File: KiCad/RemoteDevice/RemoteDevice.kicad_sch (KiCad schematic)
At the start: 43 parts, among them J1 Alim, J2 CN1, Q1 Si4435, SW1 BP, SW2 BP, U1 XC9140, U2 STM32L041F6Px, U3 MCP6281, U4 ADT7410TRZ, U5 MCP6281, U6 RT606, U7 Microphone

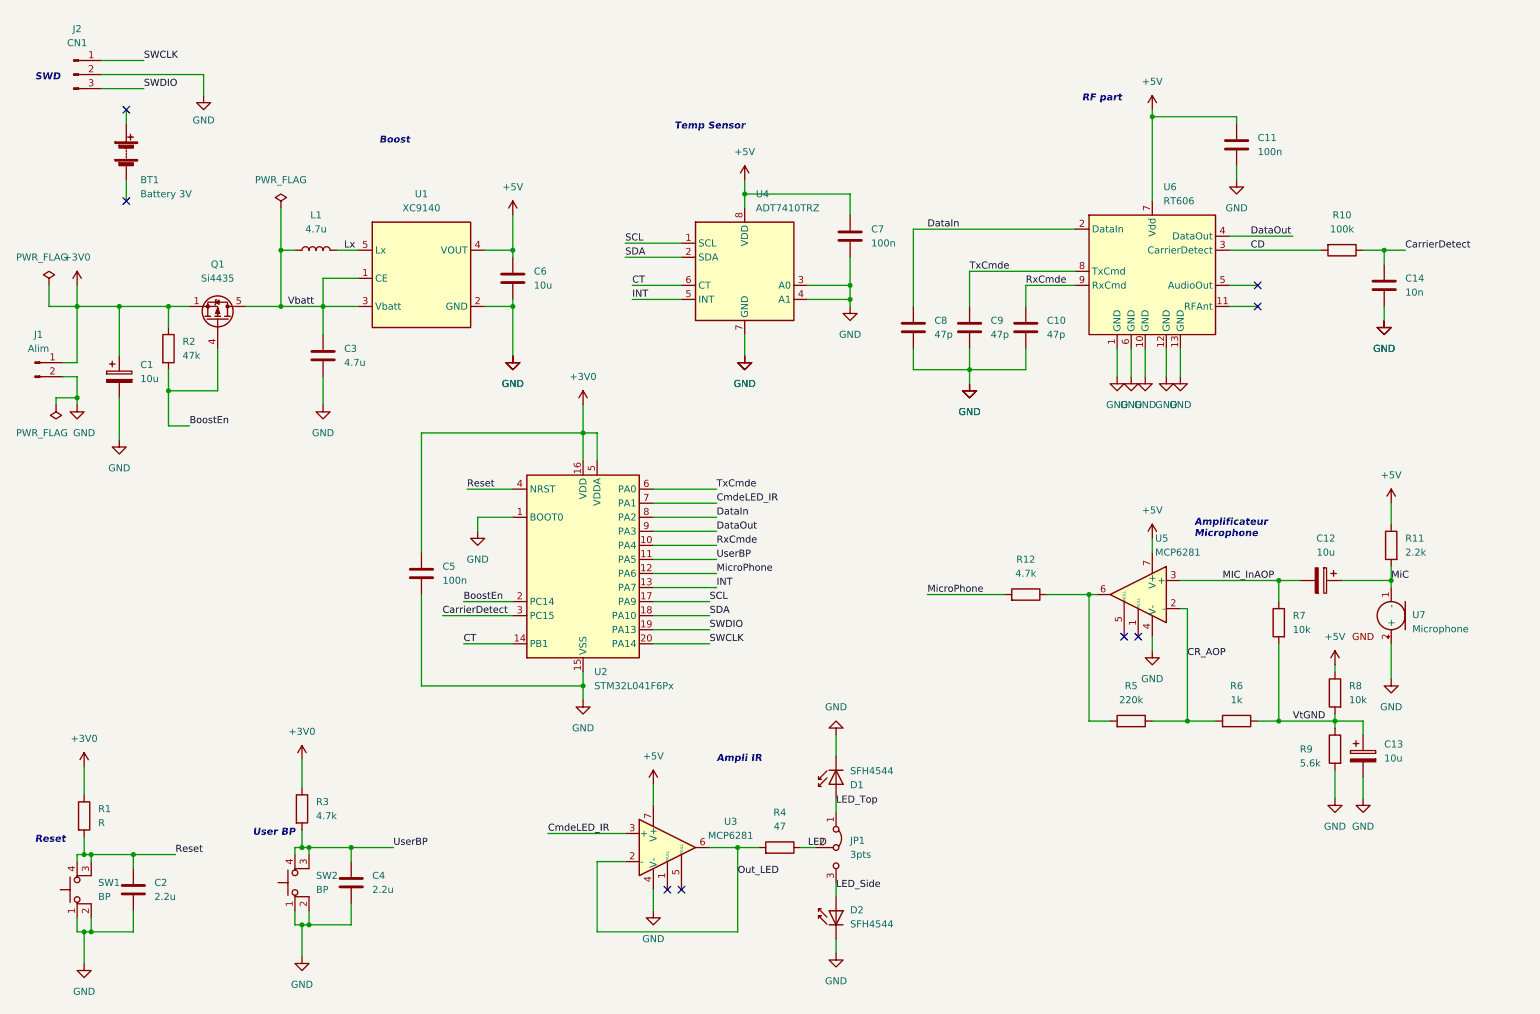
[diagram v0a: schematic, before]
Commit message: modifs schéma faites, reste à faire l'association pour la netlist. Il manque aussi le Xbee
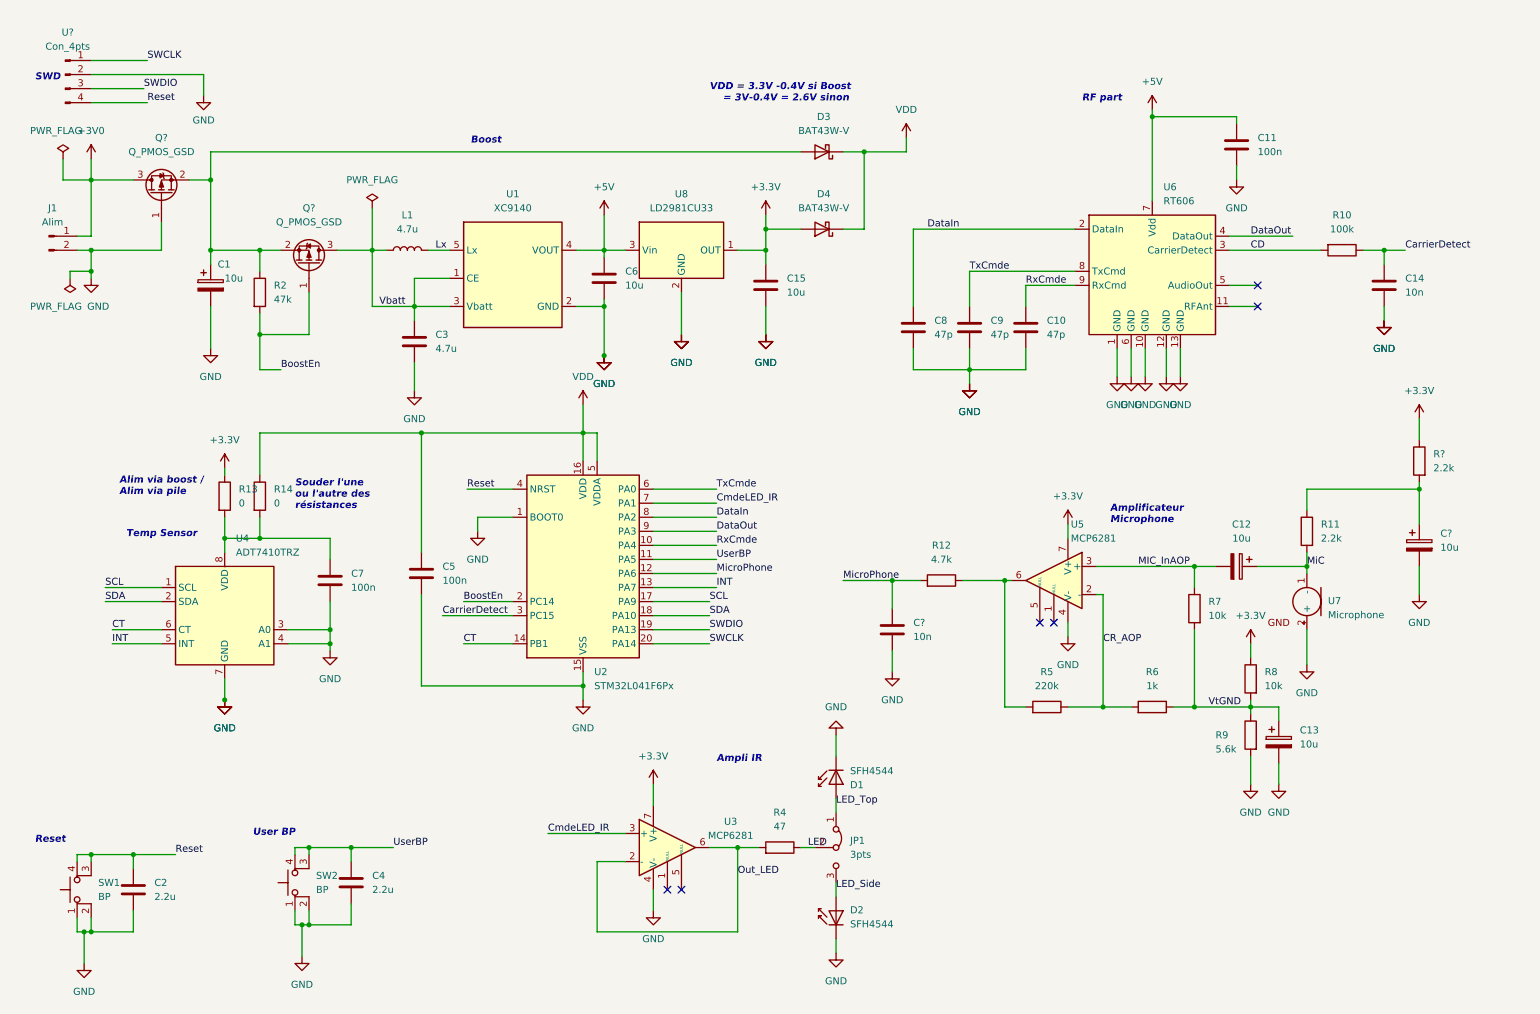
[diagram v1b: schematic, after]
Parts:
- removed BT1: Battery 3V, Battery:BatteryHolder_Keystone_2468_2xAAA, symbol Device:Battery
- removed J2: CN1, LibKiCad_PjtDeviceManagePV:PinHeader3pts, symbol Connector:Conn_01x03_Male
- removed Q1: Si4435, Package_SO:PowerPAK_SO-8_Single, symbol Transistor_FET:Si7141DP
- removed R1: R, Resistor_SMD:R_1206_3216Metric, symbol Device:R
- removed R3: 4.7k, Resistor_SMD:R_1206_3216Metric, symbol Device:R
- added C15: 10u, Capacitor_SMD:C_1812_4532Metric, symbol Device:C
- added C?: 10u, Capacitor_Tantalum_SMD:CP_EIA-7132-20_AVX-U, symbol Device:C_Polarized
- added C?: 10n, Capacitor_SMD:C_1206_3216Metric, symbol Device:C
- added D3, D4: BAT43W-V, Diode_SMD:D_SOD-123, symbol Diode:BAT43W-V
- added Q? (x2): Q_PMOS_GSD, symbol Device:Q_PMOS_GSD
- added R13, R14: 0, Resistor_SMD:R_1206_3216Metric, symbol Device:R
- added R?: 2.2k, Resistor_SMD:R_1206_3216Metric, symbol Device:R
- added U8: LD2981CU33, Package_TO_SOT_SMD:SOT-89-3_Handsoldering, symbol LibKiCad_PjtDeviceManagePV:LD2981CU33
- added U?: Con_4pts, LibKiCad_PjtDeviceManagePV:PinHeader4pts, symbol LibKiCad_PjtDeviceManagePV:Con_4pts
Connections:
- net +3V0: now also Q?.3 (D); no longer C1.1, C5.1, R2.1, U2.16 (VDD), U2.5 (VDDA)
- net +5V: now also U8.3 (Vin); no longer C7.1, R11.1, R8.1, U3.7 (V+), U4.8 (VDD), U5.7 (V+)
- net BoostEn: now also Q?.1 (G)
- net GND: now also C15.2, C?.2, C?.2, Q?.1 (G), U8.2 (GND), U?.2
- net MicroPhone: now also C?.1
- net Reset: now also U?.4
- net SWCLK: now also U?.1
- net SWDIO: now also U?.3
- net Vbatt: now also Q?.3 (D)
- new net: C7.1, R13.2, R14.2, U4.8 (VDD)
- new net: C?.1, R11.1, R?.2
- new net: C1.1, D3.2 (A), Q?.2 (S), Q?.2 (S), R2.1
- new net +3V3: C15.1, D4.2 (A), R13.1, R8.1, R?.1, U3.7 (V+), U5.7 (V+), U8.1 (OUT)
- new net VDD: C5.1, D3.1 (K), D4.1 (K), R14.1, U2.16 (VDD), U2.5 (VDDA)
- no-connect marks 8 -> 6
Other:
- note added: "Alim via boost / Alim via pile"
- note added: "Souder l'une ou l'autre des résistances"
- note added: "VDD = 3.3V -0.4V si Boost = 3V-0.4V = 2.6V sinon"
- moved on the sheet: C1, C12, C13, C3, C6, C7, J1, L1, R11, R12, R2, R5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

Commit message: schéma finalisé, prise en compte des modifs indiquées dans AfairePCB.txt. Prêt pour nouveau PCB
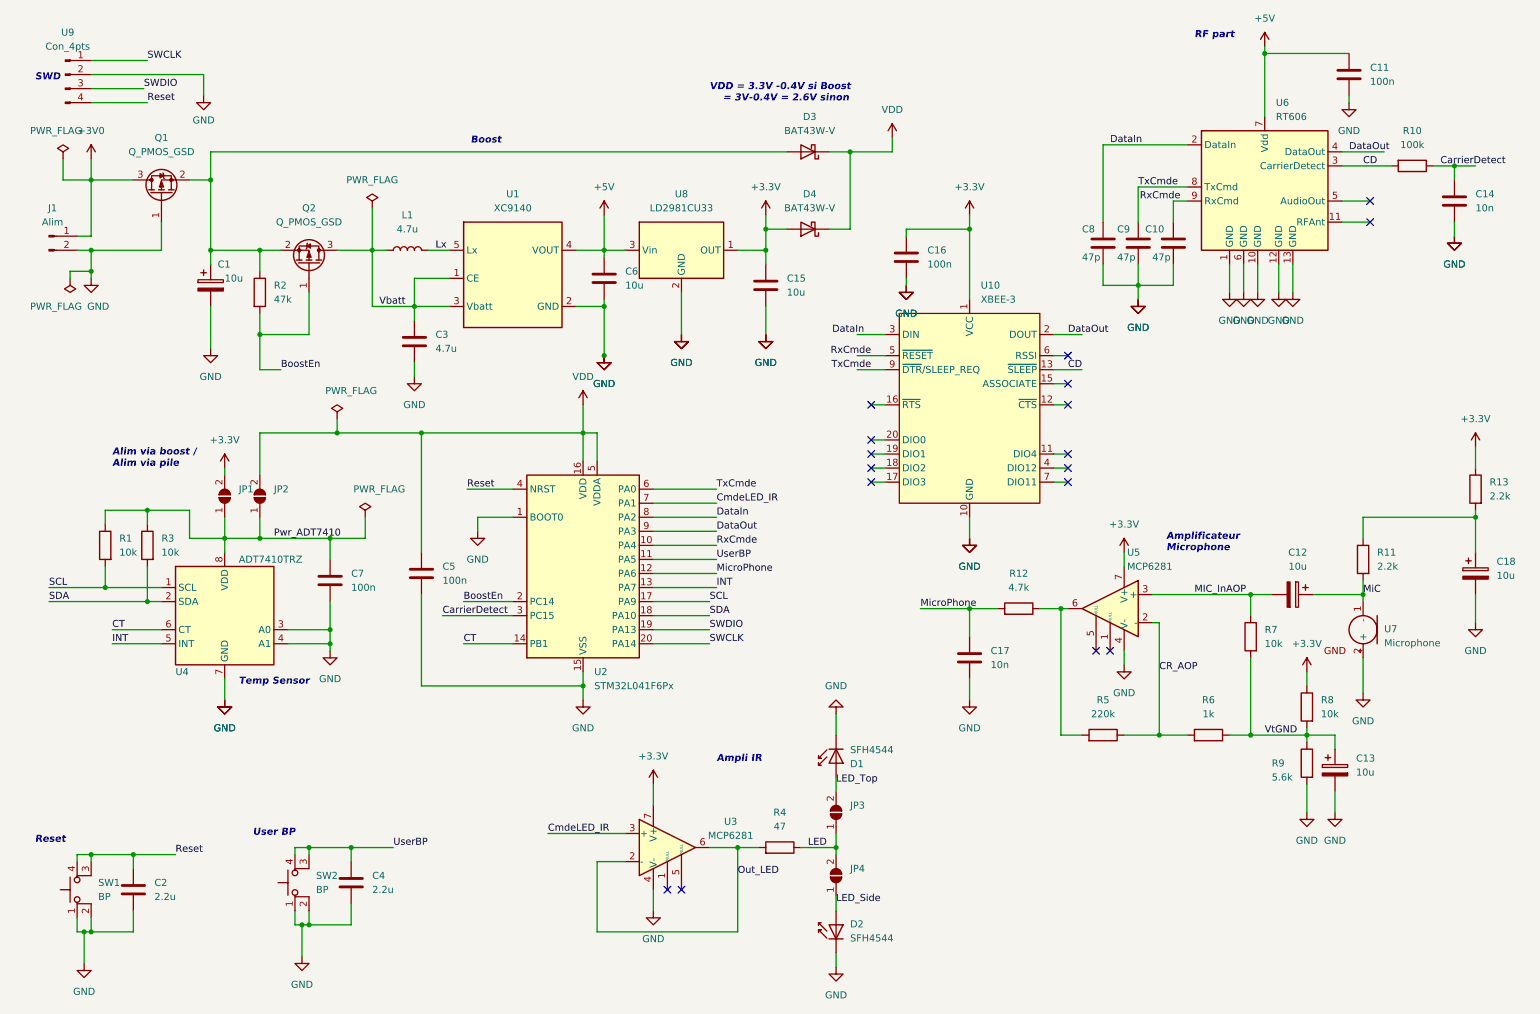
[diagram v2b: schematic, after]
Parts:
- removed JP1: 3pts, LibKiCad_PjtDeviceManagePV:PinHeader3pts, symbol Jumper:Jumper_3_Bridged12
- removed R13, R14: 0, Resistor_SMD:R_1206_3216Metric, symbol Device:R
- added C16: 100n, Capacitor_SMD:C_1206_3216Metric, symbol Device:C
- added JP1, JP2, JP3, JP4: SolderJumper_2_Open, Jumper:SolderJumper-2_P1.3mm_Open_TrianglePad1.0x1.5mm, symbol Jumper:SolderJumper_2_Open
- added R1, R3: 10k, Resistor_SMD:R_1206_3216Metric, symbol Device:R
- added U10: XBEE-3, INSA:XBEE-3-TH, symbol Insa:XBEE-3
- gave numbers to parts that had none: 6
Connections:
- net +3V3: now also C16.1, JP1.2 (B), U10.1 (VCC)
- net CD: now also U10.13 (~{SLEEP})
- net DataIn: now also U10.3 (DIN)
- net DataOut: now also U10.2 (DOUT)
- net GND: now also C16.2, U10.10 (GND)
- net LED: now also JP3.1 (A), JP4.2 (B)
- net LED_Side: now also JP4.1 (A)
- net LED_Top: now also JP3.2 (B)
- net RxCmde: now also U10.5 (~{RESET})
- net SCL: now also R1.2
- net SDA: now also R3.2
- net TxCmde: now also U10.9 (~{DTR}/SLEEP_REQ)
- net VDD: now also JP2.2 (B)
- net Pwr_ADT7410: now reaches C7.1, U4.8 (VDD)
- net Pwr_ADT7410: now also JP1.1 (A), JP2.1 (A), R1.1, R3.1
- no-connect marks 6 -> 17
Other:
- note removed: "Souder l'une ou l'autre des résistances"
- moved on the sheet: C10, C11, C12, C13, C14, C17, C18, C8, C9, D1, D2, D3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

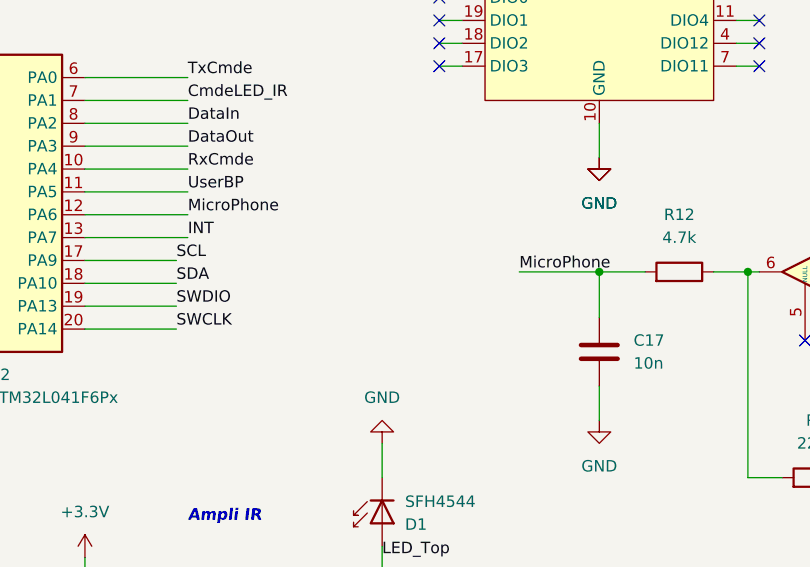
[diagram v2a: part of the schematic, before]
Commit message: routage commencé. ALim OK placer les deux diodes, étudier l'alim particulière uC et Temp Sensor
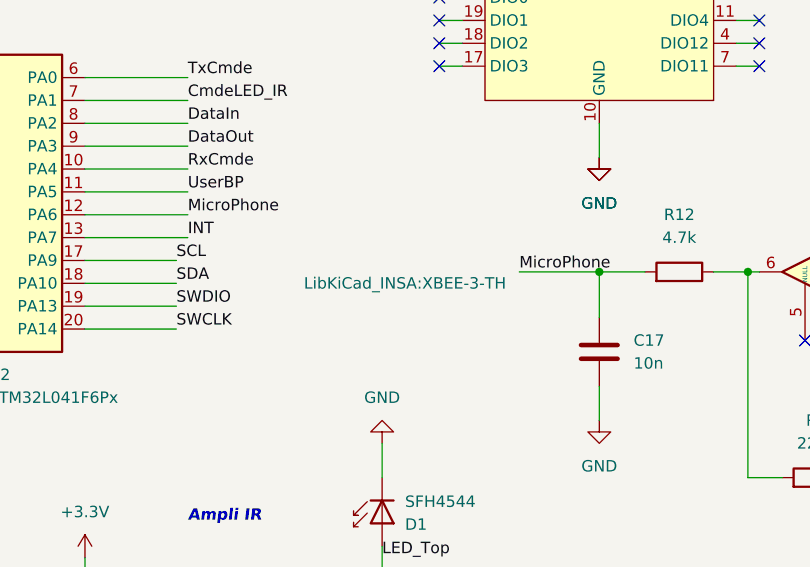
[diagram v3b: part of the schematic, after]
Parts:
- Q1, Q2: footprint (none) -> Package_TO_SOT_SMD:SOT-23
- U10: footprint INSA:XBEE-3-TH -> LibKiCad_INSA:XBEE-3-TH
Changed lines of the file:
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@@
       (effects (font (size 1.27 1.27)) (justify left))
     )
-    (property "Footprint" "INSA:XBEE-3-TH" (id 2) (at 163.83 123.19 0)
-      (effects (font (size 1.27 1.27)) hide)
-    )
+    (property "Footprint" "LibKiCad_INSA:XBEE-3-TH" (id 2) (at 163.83 123.19 0))
     (property "Datasheet" "" (id 3) (at 163.83 123.19 0)
       (effects (font (size 1.27 1.27)) hide)
@@
     (property "Reference" "Q1" (id 0) (at 39.37 36.83 90))
     (property "Value" "Q_PMOS_GSD" (id 1) (at 39.37 39.37 90))
-    (property "Footprint" "" (id 2) (at 36.83 41.91 0)
+    (property "Footprint" "Package_TO_SOT_SMD:SOT-23" (id 2) (at 36.83 41.91 0)
       (effects (font (size 1.27 1.27)) hide)
     )
@@
     (property "Reference" "Q2" (id 0) (at 66.04 49.53 90))
     (property "Value" "Q_PMOS_GSD" (id 1) (at 66.04 52.07 90))
-    (property "Footprint" "" (id 2) (at 68.58 54.61 0)
+    (property "Footprint" "Package_TO_SOT_SMD:SOT-23" (id 2) (at 68.58 54.61 0)
       (effects (font (size 1.27 1.27)) hide)
     )
@@
     )
     (path "/309ab532-fbfc-4b78-b9be-dd62da22f1c1"
-      (reference "Q1") (unit 1) (value "Q_PMOS_GSD") (footprint "")
+      (reference "Q1") (unit 1) (value "Q_PMOS_GSD") (footprint "Package_TO_SOT_SMD:SOT-23")
     )
     (path "/70d76e55-908c-4803-85fa-52541360684c"
-      (reference "Q2") (unit 1) (value "Q_PMOS_GSD") (footprint "")
+      (reference "Q2") (unit 1) (value "Q_PMOS_GSD") (footprint "Package_TO_SOT_SMD:SOT-23")
     )
     (path "/64237b66-5629-4cfd-865f-19c8e3222e7e"
@@
     )
     (path "/08ba03eb-af60-4fcf-b210-5b04d3c9a823"
-      (reference "U10") (unit 1) (value "XBEE-3") (footprint "INSA:XBEE-3-TH")
-    )
-  )
+      (reference "U10") (unit 1) (value "XBEE-3") (footprint "LibKiCad_INSA:XBEE-3-TH")
+    )
+  )
